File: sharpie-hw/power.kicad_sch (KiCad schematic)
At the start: 21 parts, among them J2 Conn_01x02_MountingPin, J5 Conn_01x14, J6 LS021B7DD02, U1 TPS7A2533, U2 TPS7A2501, U7 AP3602A

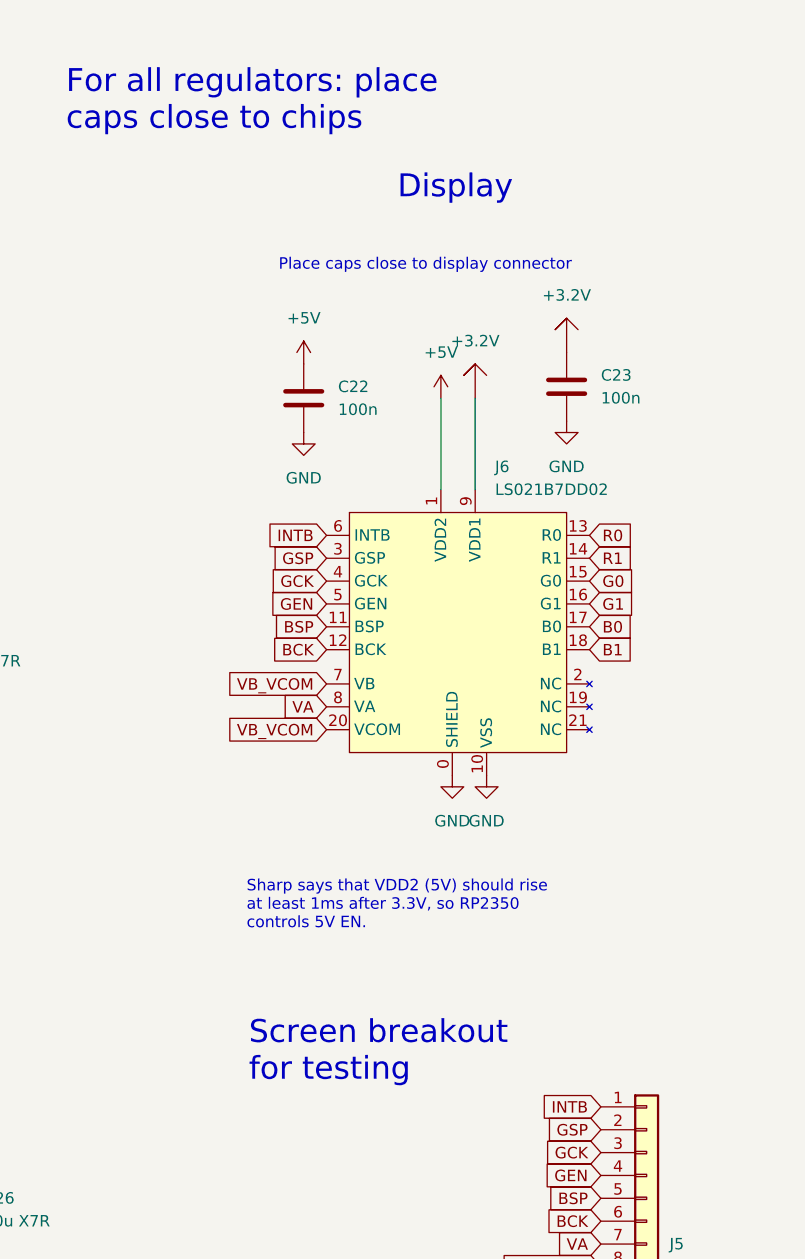
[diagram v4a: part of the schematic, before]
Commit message: Fix some BOM entries and routing choices.
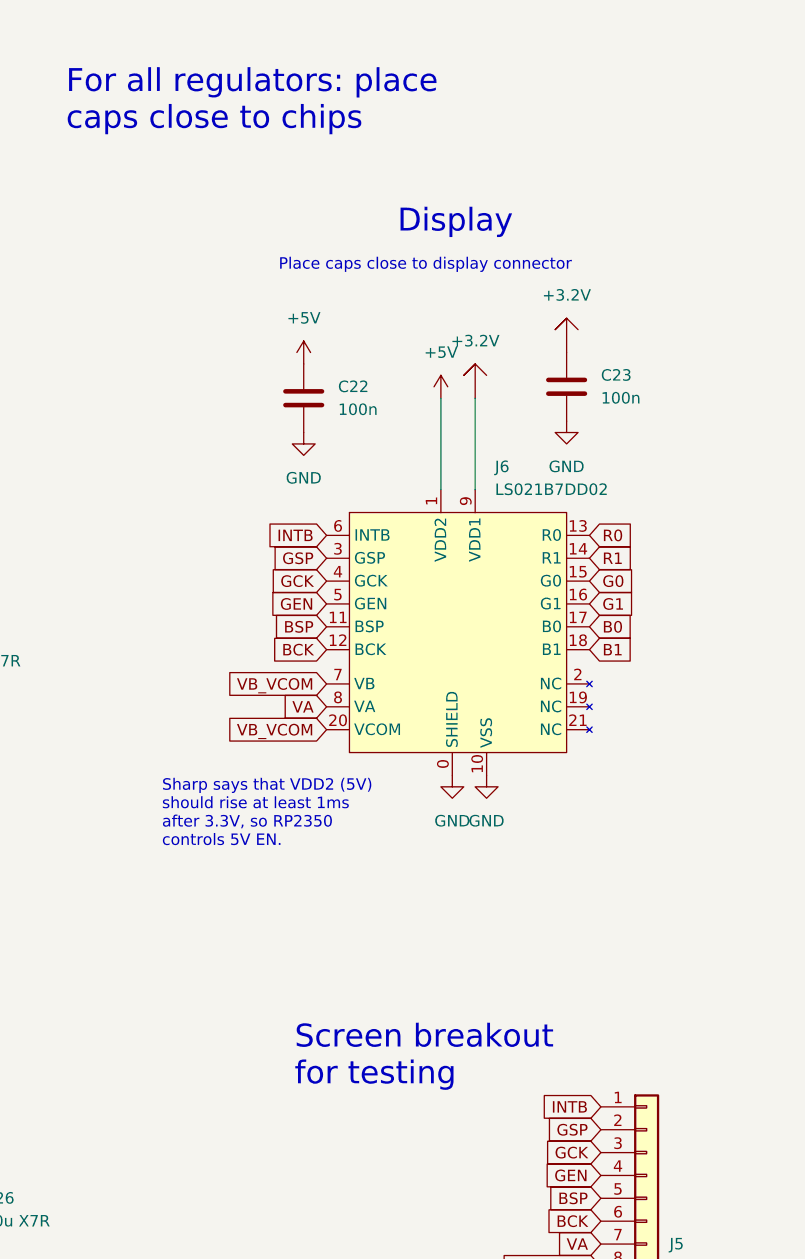
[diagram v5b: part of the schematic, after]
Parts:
- U1: JLCPCB Part # C2864326 -> C2867820
- U2: JLCPCB Part # C2867820 -> C2864326
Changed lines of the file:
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@@
 	(text "Display"
 		(exclude_from_sim no)
-		(at 223.774 33.782 0)
+		(at 223.774 37.592 0)
 		(effects
 			(font
@@
 		)
 	)
-	(text "Sharp says that VDD2 (5V) should rise\nat least 1ms after 3.3V, so RP2350 \ncontrols 5V EN."
-		(exclude_from_sim no)
-		(at 207.01 113.538 0)
+	(text "Sharp says that VDD2 (5V) \nshould rise at least 1ms \nafter 3.3V, so RP2350 \ncontrols 5V EN."
+		(exclude_from_sim no)
+		(at 197.612 103.378 0)
 		(effects
 			(font
@@
 	(text "Screen breakout\nfor testing"
 		(exclude_from_sim no)
-		(at 207.264 129.794 0)
+		(at 212.344 130.302 0)
 		(effects
 			(font
@@
 			)
 		)
-		(property "JLCPCB Part #" "C2864326"
+		(property "JLCPCB Part #" "C2867820"
 			(at 137.16 40.64 0)
 			(effects
@@
 			)
 		)
-		(property "JLCPCB Part #" "C2867820"
+		(property "JLCPCB Part #" "C2864326"
 			(at 138.43 82.55 0)
 			(effects

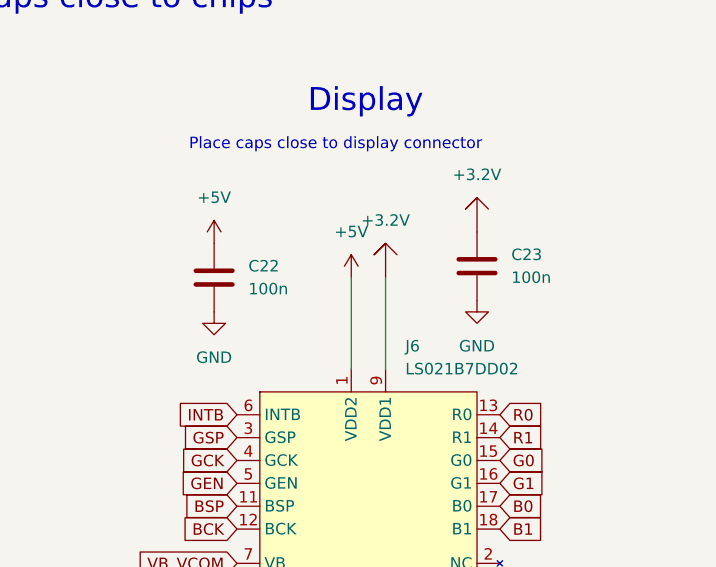
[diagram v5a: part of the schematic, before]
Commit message: Adjust display regulators to match datasheet, so they're now 1u 0805.
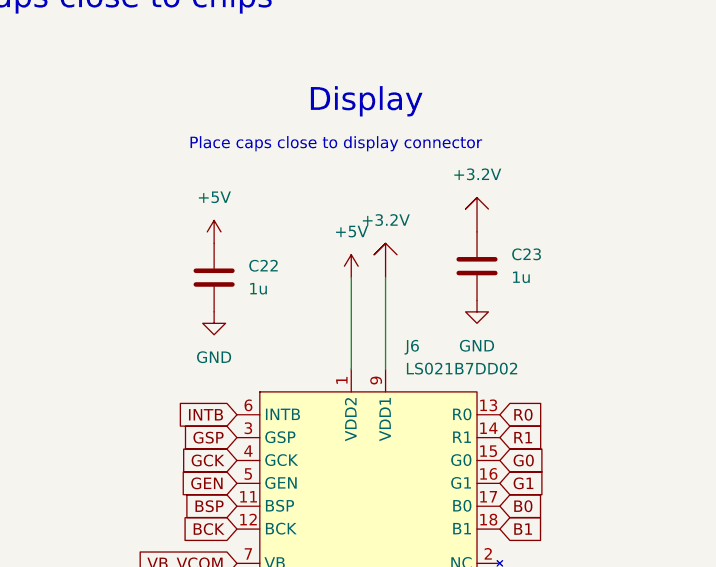
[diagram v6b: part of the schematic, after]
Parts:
- C22, C23: value 100n -> 1u; footprint Capacitor_SMD:C_0402_1005Metric -> Capacitor_SMD:C_0805_2012Metric; JLCPCB Part # C1525 -> C94122
- C25, C26: JLCPCB Part # C326595 -> C94122
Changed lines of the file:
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@@
 			)
 		)
-		(property "Value" "100n"
+		(property "Value" "1u"
 			(at 217.17 58.4199 0)
 			(effects
@@
 			)
 		)
-		(property "Footprint" "Capacitor_SMD:C_0402_1005Metric"
+		(property "Footprint" "Capacitor_SMD:C_0805_2012Metric"
 			(at 214.3252 60.96 0)
 			(effects
@@
 			)
 		)
-		(property "JLCPCB Part #" "C1525"
+		(property "JLCPCB Part #" "C94122"
 			(at 213.36 57.15 0)
 			(effects
@@
 			)
 		)
-		(property "JLCPCB Part #" "C326595"
+		(property "JLCPCB Part #" "C94122"
 			(at 111.76 147.32 0)
 			(effects
@@
 			)
 		)
-		(property "Value" "100n"
+		(property "Value" "1u"
 			(at 246.38 57.1499 0)
 			(effects
@@
 			)
 		)
-		(property "Footprint" "Capacitor_SMD:C_0402_1005Metric"
+		(property "Footprint" "Capacitor_SMD:C_0805_2012Metric"
 			(at 243.5352 59.69 0)
 			(effects
@@
 			)
 		)
-		(property "JLCPCB Part #" "C1525"
+		(property "JLCPCB Part #" "C94122"
 			(at 242.57 55.88 0)
 			(effects
@@
 			)
 		)
-		(property "JLCPCB Part #" "C326595"
+		(property "JLCPCB Part #" "C94122"
 			(at 173.99 147.32 0)
 			(effects

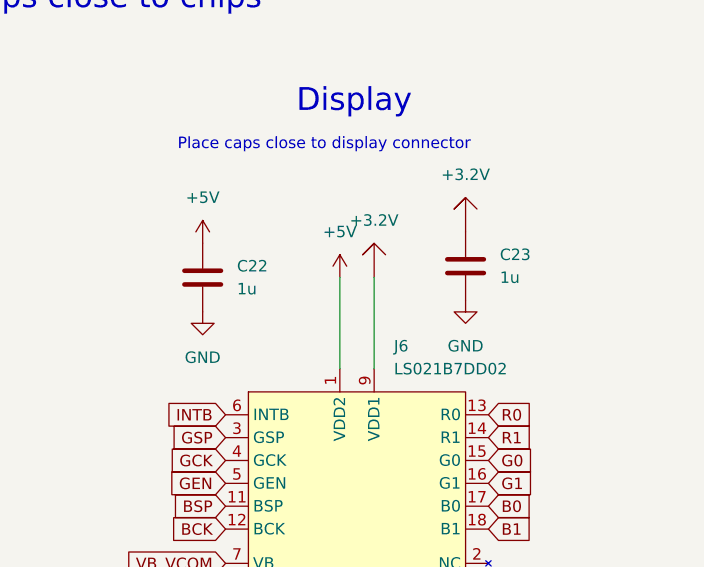
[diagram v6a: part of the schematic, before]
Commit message: Adjust orientation of necessary parts for JLCPCB assembly.
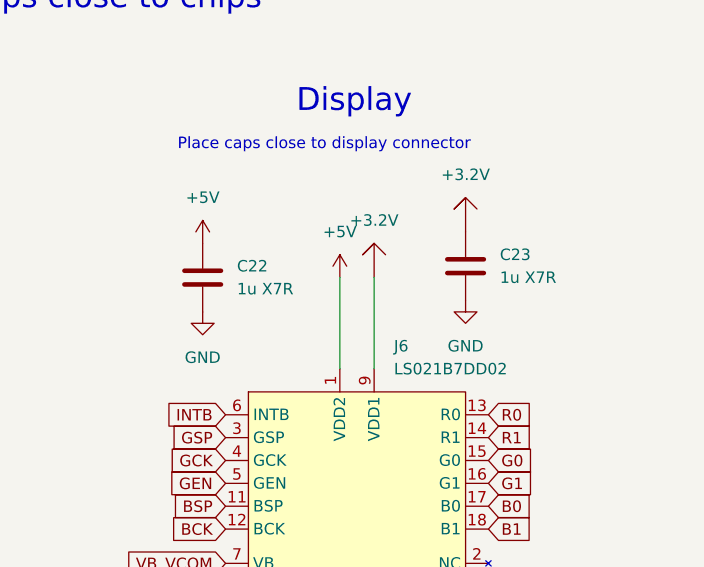
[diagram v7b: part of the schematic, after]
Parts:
- C22, C23: value 1u -> 1u X7R
- C25: JLCPCB Part # C94122 -> C326595
- J1: JLCPCB Position Offset (none) -> -1,0
- J2: FT Rotation Offset (none) -> 180
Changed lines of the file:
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@@
 			)
 		)
+		(property "FT Rotation Offset" "180"
+			(at 35.56 114.3 0)
+			(effects
+				(font
+					(size 1.27 1.27)
+				)
+				(hide yes)
+			)
+		)
 		(pin "2"
 		)
@@
 			)
 		)
-		(property "Value" "1u"
+		(property "Value" "1u X7R"
 			(at 217.17 58.4199 0)
 			(effects
@@
 			)
 		)
+		(property "JLCPCB Position Offset" "-1,0"
+			(at 33.02 49.53 0)
+			(effects
+				(font
+					(size 1.27 1.27)
+				)
+				(hide yes)
+			)
+		)
 		(pin "B12"
 		)
@@
 			)
 		)
-		(property "JLCPCB Part #" "C94122"
+		(property "JLCPCB Part #" "C326595"
 			(at 111.76 147.32 0)
 			(effects
@@
 			)
 		)
-		(property "Value" "1u"
+		(property "Value" "1u X7R"
 			(at 246.38 57.1499 0)
 			(effects

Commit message: Move to as many JLCPCB basic parts as possible and remove user button.
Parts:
- C1, C2, C22, C23, C24: JLCPCB Part # C94122 -> C28323
- C25: JLCPCB Part # C326595 -> C15850
- C26: JLCPCB Part # C94122 -> C15850
- C3, C4: JLCPCB Part # C107128 -> C377773
- J1: FT Position Offset (none) -> 0,2.4765; JLCPCB Position Offset -1,0 -> (none)
- R12: JLCPCB Part # C25530 -> C25741
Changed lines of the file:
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@@
 (kicad_sch
-	(version 20231120)
+	(version 20250114)
 	(generator "eeschema")
-	(generator_version "8.0")
+	(generator_version "9.0")
 	(paper "USLetter")
+	(text "basic 5V/3A sink, from\nhttps://hackaday.com/2023/08/07/\nall-about-usb-c-example-circuits/\nS1 (shield) pin has been removed\nto match footprint."
+		(exclude_from_sim no)
+		(at 19.304 84.582 0)
+		(effects
+			(font
+				(size 1.27 1.27)
+			)
+			(justify left)
+		)
+	)
+	(text "Place flying cap as close\nto chip as possible"
+		(exclude_from_sim no)
+		(at 164.338 164.592 0)
+		(effects
+			(font
+				(size 1.27 1.27)
+			)
+			(justify left)
+		)
+	)
+	(text "3.3V regulator"
+		(exclude_from_sim no)
+		(at 123.952 17.78 0)
+		(effects
+			(font
+				(size 2.54 2.54)
+			)
+			(justify left)
+		)
+	)
+	(text "Following Adafruit battery\npinout: p1 = GND, p2 = VCC"
+		(exclude_from_sim no)
+		(at 19.05 134.874 0)
+		(effects
+			(font
+				(size 1.27 1.27)
+			)
+			(justify left)
+		)
+	)
+	(text "V_out = V_FB*(1 + R1/R2)\n3.209 = 1.24*(1 + 1.62M/1.02M)\n1% Rs, R1/R2 ideal for 3.2V = 1.66,\nactual = 1.588\nR1+R2 for 3.2V = 3.3M, actual=2.64M\n\nregulator is 300 mA, which is more\nthan enough (screen is negligable\nand RP2350 can sink/source up to 100 mA)"
+		(exclude_from_sim no)
+		(at 106.426 107.188 0)
+		(effects
+			(font
+				(size 1.27 1.27)
+			)
+			(justify left)
+		)
+	)
+	(text "EN must not be floating,\nand it needs to stay low until\nwe turn it on."
+		(exclude_from_sim no)
+		(at 79.248 141.732 0)
+		(effects
+			(font
+				(size 1.27 1.27)
+			)
+			(justify left)
+		)
+	)
+	(text "3.2V regulator"
+		(exclude_from_sim no)
+		(at 123.444 63.754 0)
+		(effects
+			(font
+				(size 2.54 2.54)
+			)
+			(justify left)
+		)
+	)
+	(text "Display"
+		(exclude_from_sim no)
+		(at 223.774 37.592 0)
+		(effects
+			(font
+				(size 2.54 2.54)
+			)
+			(justify left)
+		)
+	)
+	(text "VCC is both VBUS from USB\nand VBAT from the battery.\nDon't attach both at the\nsame time!"
+		(exclude_from_sim no)
+		(at 70.358 61.976 0)
+		(effects
+			(font
+				(size 1.27 1.27)
+			)
+			(justify left)
+		)
+	)
+	(text "Battery"
+		(exclude_from_sim no)
+		(at 23.876 98.806 0)
+		(effects
+			(font
+				(size 2.54 2.54)
+			)
+			(justify left)
+		)
+	)
+	(text "Place caps close to display connector"
+		(exclude_from_sim no)
+		(at 210.566 42.418 0)
+		(effects
+			(font
+				(size 1.27 1.27)
+			)
+			(justify left)
+		)
+	)
+	(text "part must be TPS7A2533DRVR\n300 mA max\nTI says connect EN to VIN\nand PG to GND if unused"
+		(exclude_from_sim no)
+		(at 122.682 24.892 0)
+		(effects
+			(font
+				(size 1.27 1.27)
+			)
+			(justify left)
+		)
+	)
+	(text "For all regulators: place\ncaps close to chips"
+		(exclude_from_sim no)
+		(at 186.944 24.13 0)
+		(effects
+			(font
+				(size 2.54 2.54)
+			)
+			(justify left)
+		)
+	)
+	(text "part must be TPS2A2501DRVR\n300 mA max"
+		(exclude_from_sim no)
+		(at 122.428 69.85 0)
+		(effects
+			(font
+				(size 1.27 1.27)
+			)
+			(justify left)
+		)
+	)
+	(text "5V charge pump\nplus 5V enable"
+		(exclude_from_sim no)
+		(at 125.73 127.508 0)
+		(effects
+			(font
+				(size 2.54 2.54)
+			)
+			(justify left)
+		)
+	)
+	(text "Following Adafruit 4694, 2.7\"\nSharp memory display, we use\nan AP3602 with a 1u flying\ncap for the 5V supply.\n\nThey show this chip being used\nwith 5V input, which is its max."
+		(exclude_from_sim no)
+		(at 125.984 170.434 0)
+		(effects
+			(font
+				(size 1.27 1.27)
+			)
+			(justify left)
+		)
+	)
+	(text "Sharp says that VDD2 (5V) \nshould rise at least 1ms \nafter 3.3V, so RP2350 \ncontrols 5V EN."
+		(exclude_from_sim no)
+		(at 197.612 103.378 0)
+		(effects
+			(font
+				(size 1.27 1.27)
+			)
+			(justify left)
+		)
+	)
+	(text "Screen breakout\nfor testing"
+		(exclude_from_sim no)
+		(at 212.344 130.302 0)
+		(effects
+			(font
+				(size 2.54 2.54)
+			)
+			(justify left)
+		)
+	)
+	(text "USB-C"
+		(exclude_from_sim no)
+		(at 37.592 17.018 0)
+		(effects
+			(font
+				(size 2.54 2.54)
+			)
+			(justify left)
+		)
+	)
 	(junction
 		(at 138.43 91.44)
@@
 		)
 	)
-	(text "basic 5V/3A sink, from\nhttps://hackaday.com/2023/08/07/\nall-about-usb-c-example-circuits/\nS1 (shield) pin has been removed\nto match footprint."
-		(exclude_from_sim no)
-		(at 19.304 84.582 0)
-		(effects
-			(font
-				(size 1.27 1.27)
-			)
-			(justify left)
-		)
-	)
-	(text "Place flying cap as close\nto chip as possible"
-		(exclude_from_sim no)
-		(at 164.338 164.592 0)
-		(effects
-			(font
-				(size 1.27 1.27)
-			)
-			(justify left)
-		)
-	)
-	(text "3.3V regulator"
-		(exclude_from_sim no)
-		(at 123.952 17.78 0)
-		(effects
-			(font
-				(size 2.54 2.54)
-			)
-			(justify left)
-		)
-	)
-	(text "Following Adafruit battery\npinout: p1 = GND, p2 = VCC"
-		(exclude_from_sim no)
-		(at 19.05 134.874 0)
-		(effects
-			(font
-				(size 1.27 1.27)
-			)
-			(justify left)
-		)
-	)
-	(text "V_out = V_FB*(1 + R1/R2)\n3.209 = 1.24*(1 + 1.62M/1.02M)\n1% Rs, R1/R2 ideal for 3.2V = 1.66,\nactual = 1.588\nR1+R2 for 3.2V = 3.3M, actual=2.64M\n\nregulator is 300 mA, which is more\nthan enough (screen is negligable\nand RP2350 can sink/source up to 100 mA)"
-		(exclude_from_sim no)
-		(at 106.426 107.188 0)
-		(effects
-			(font
-				(size 1.27 1.27)
-			)
-			(justify left)
-		)
-	)
-	(text "EN must not be floating,\nand it needs to stay low until\nwe turn it on."
-		(exclude_from_sim no)
-		(at 79.248 141.732 0)
-		(effects
-			(font
-				(size 1.27 1.27)
-			)
-			(justify left)
-		)
-	)
-	(text "3.2V regulator"
-		(exclude_from_sim no)
-		(at 123.444 63.754 0)
-		(effects
-			(font
-				(size 2.54 2.54)
-			)
-			(justify left)
-		)
-	)
-	(text "Display"
-		(exclude_from_sim no)
-		(at 223.774 37.592 0)
-		(effects
-			(font
-				(size 2.54 2.54)
-			)
-			(justify left)
-		)
-	)
-	(text "VCC is both VBUS from USB\nand VBAT from the battery.\nDon't attach both at the\nsame time!"
-		(exclude_from_sim no)
-		(at 70.358 61.976 0)
-		(effects
-			(font
-				(size 1.27 1.27)
-			)
-			(justify left)
-		)
-	)
-	(text "Battery"
-		(exclude_from_sim no)
-		(at 23.876 98.806 0)
-		(effects
-			(font
-				(size 2.54 2.54)
-			)
-			(justify left)
-		)
-	)
-	(text "Place caps close to display connector"
-		(exclude_from_sim no)
-		(at 210.566 42.418 0)
-		(effects
-			(font
-				(size 1.27 1.27)
-			)
-			(justify left)
-		)
-	)
-	(text "part must be TPS7A2533DRVR\n300 mA max\nTI says connect EN to VIN\nand PG to GND if unused"
-		(exclude_from_sim no)
-		(at 122.682 24.892 0)
-		(effects
-			(font
-				(size 1.27 1.27)
-			)
-			(justify left)
-		)
-	)
-	(text "For all regulators: place\ncaps close to chips"
-		(exclude_from_sim no)
-		(at 186.944 24.13 0)
-		(effects
-			(font
-				(size 2.54 2.54)
-			)
-			(justify left)
-		)
-	)
-	(text "part must be TPS2A2501DRVR\n300 mA max"
-		(exclude_from_sim no)
-		(at 122.428 69.85 0)
-		(effects
-			(font
-				(size 1.27 1.27)
-			)
-			(justify left)
-		)
-	)
-	(text "5V charge pump\nplus 5V enable"
-		(exclude_from_sim no)
-		(at 125.73 127.508 0)
-		(effects
-			(font
-				(size 2.54 2.54)
-			)
-			(justify left)
-		)
-	)
-	(text "Following Adafruit 4694, 2.7\"\nSharp memory display, we use\nan AP3602 with a 1u flying\ncap for the 5V supply.\n\nThey show this chip being used\nwith 5V input, which is its max."
-		(exclude_from_sim no)
-		(at 125.984 170.434 0)
-		(effects
-			(font
-				(size 1.27 1.27)
-			)
-			(justify left)
-		)
-	)
-	(text "Sharp says that VDD2 (5V) \nshould rise at least 1ms \nafter 3.3V, so RP2350 \ncontrols 5V EN."
-		(exclude_from_sim no)
-		(at 197.612 103.378 0)
-		(effects
-			(font
-				(size 1.27 1.27)
-			)
-			(justify left)
-		)
-	)
-	(text "Screen breakout\nfor testing"
-		(exclude_from_sim no)
-		(at 212.344 130.302 0)
-		(effects
-			(font
-				(size 2.54 2.54)
-			)
-			(justify left)
-		)
-	)
-	(text "USB-C"
-		(exclude_from_sim no)
-		(at 37.592 17.018 0)
-		(effects
-			(font
-				(size 2.54 2.54)
-			)
-			(justify left)
-		)
-	)
 	(global_label "B1"
 		(shape input)
@@
 			)
 		)
-		(property "JLCPCB Part #" "C107128"
+		(property "JLCPCB Part #" "C377773"
 			(at 170.18 85.09 0)
 			(effects
@@
 			)
 		)
-		(property "JLCPCB Part #" "C94122"
+		(property "JLCPCB Part #" "C28323"
 			(at 161.29 157.48 0)
 			(effects
@@
 			)
 		)
-		(property "JLCPCB Part #" "C107128"
+		(property "JLCPCB Part #" "C377773"
 			(at 154.94 43.18 0)
 			(effects
@@
 			)
 		)
-		(property "JLCPCB Part #" "C94122"
+		(property "JLCPCB Part #" "C28323"
 			(at 213.36 57.15 0)
 			(effects
@@
 			)
 		)
-		(property "JLCPCB Part #" "C25530"
+		(property "JLCPCB Part #" "C25741"
 			(at 95.25 152.4 0)
 			(effects
@@
 			)
 		)
-		(property "JLCPCB Position Offset" "-1,0"
+		(property "FT Position Offset" "0,2.4765"
 			(at 33.02 49.53 0)
 			(effects
@@
 			)
 		)
-		(property "JLCPCB Part #" "C94122"
+		(property "JLCPCB Part #" "C28323"
 			(at 116.84 85.09 0)
 			(effects
@@
 			)
 		)
-		(property "JLCPCB Part #" "C326595"
+		(property "JLCPCB Part #" "C15850"
 			(at 111.76 147.32 0)
 			(effects
@@
 			)
 		)
-		(property "JLCPCB Part #" "C94122"
+		(property "JLCPCB Part #" "C28323"
 			(at 242.57 55.88 0)
 			(effects
@@
 			)
 		)
-		(property "JLCPCB Part #" "C94122"
+		(property "JLCPCB Part #" "C15850"
 			(at 173.99 147.32 0)
 			(effects
@@
 			)
 		)
-		(property "JLCPCB Part #" "C94122"
+		(property "JLCPCB Part #" "C28323"
 			(at 116.84 43.18 0)
 			(effects
